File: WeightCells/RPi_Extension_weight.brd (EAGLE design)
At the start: 80 x 50 mm, 32 parts, among them U1 AD7730BRUZ, U2 AD7730BRUZ, U3 AD7730BRUZ, U4 AD7730BRUZ, U5 AD7730BRUZ, U6 AD7730BRUZ, U7 AD7730BRUZ, U8 AD7730BRUZ, U9 STM32F103RCT6

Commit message: updated pcbs
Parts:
- added C10, C9: 0.1uf, rcl:C0603
- renumbered U$1 to Y2, U$2 to Y1
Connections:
- net DVCC: now also C10.1, C9.1
- net GND: now also C10.2, C9.2
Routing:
- net DVCC: track 282.6 -> 286.5 mm
- net U5_AIN1_+: track 24.7 -> 23.6 mm
- net U5_AIN1_-: track 21.9 -> 21.0 mm
- net U6_AIN1_+: track 18.4 -> 17.5 mm
- net +5V: track 151.1 -> 151.8 mm
- net MOSI: track 52.4 -> 51.9 mm

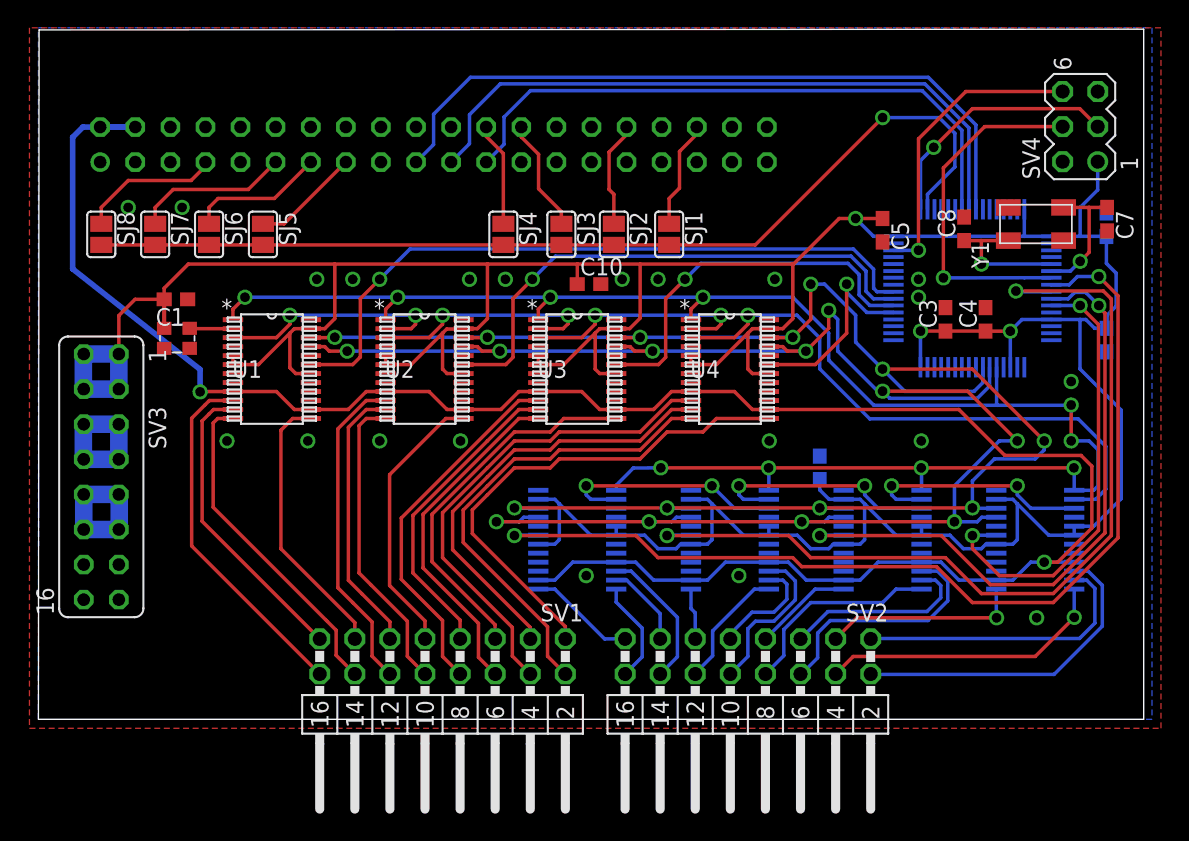
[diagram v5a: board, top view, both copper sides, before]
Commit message: added address lines up to 16 to loadcell board
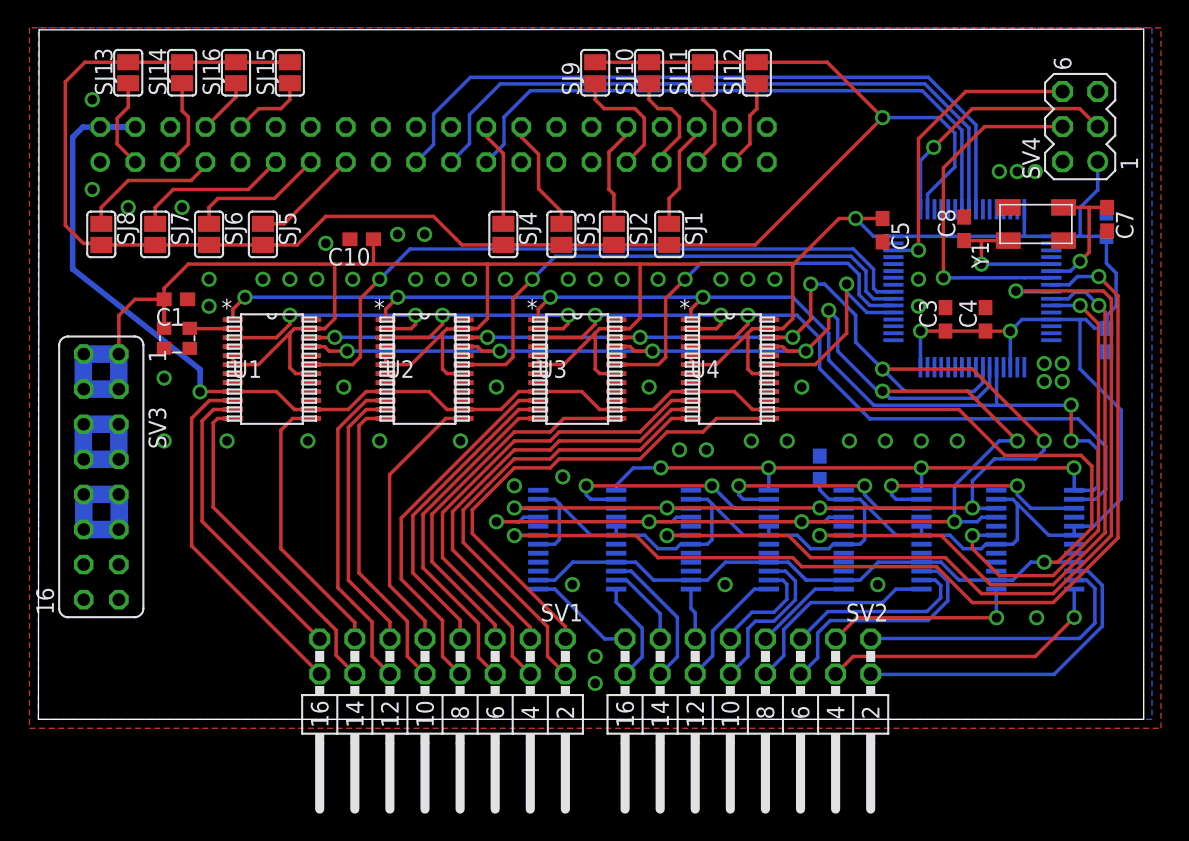
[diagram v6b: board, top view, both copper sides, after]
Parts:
- added SJ10, SJ11, SJ12, SJ13, SJ14, SJ15, SJ16, SJ9: (no value), jumper:SJ
- moved C10 16.8 mm to (23.4, 34.8), turned to 180 degrees
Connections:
- new net N$1: SJ12.1, SV5.37
- new net N$10: SJ14.1, SV5.5
- new net N$4: SJ11.1, SV5.35
- new net N$5: SJ10.1, SV5.33
- new net N$6: SJ9.1, SV5.31
- new net N$7: SJ16.1, SV5.8
- new net N$8: SJ15.1, SV5.10
- new net N$9: SJ13.1, SV5.3
- net SS_STACK: now also SJ10.2, SJ11.2, SJ12.2, SJ13.2, SJ14.2, SJ15.2, SJ16.2, SJ9.2
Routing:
- net SS_STACK: track 72.4 -> 127.0 mm
- net N$6: track 0.00 -> 9.02 mm
- net N$5: track 0.00 -> 7.70 mm
- net N$4: track 0.00 -> 6.60 mm
- net N$9: track 0.00 -> 6.58 mm
- net N$1: track 0.00 -> 6.46 mm
- net N$10: track 0.00 -> 6.43 mm
- net N$8: track 0.00 -> 5.58 mm
- net N$7: track 0.00 -> 4.10 mm

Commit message: created gerber files for adc and load cell board and did some retouch on load cell board
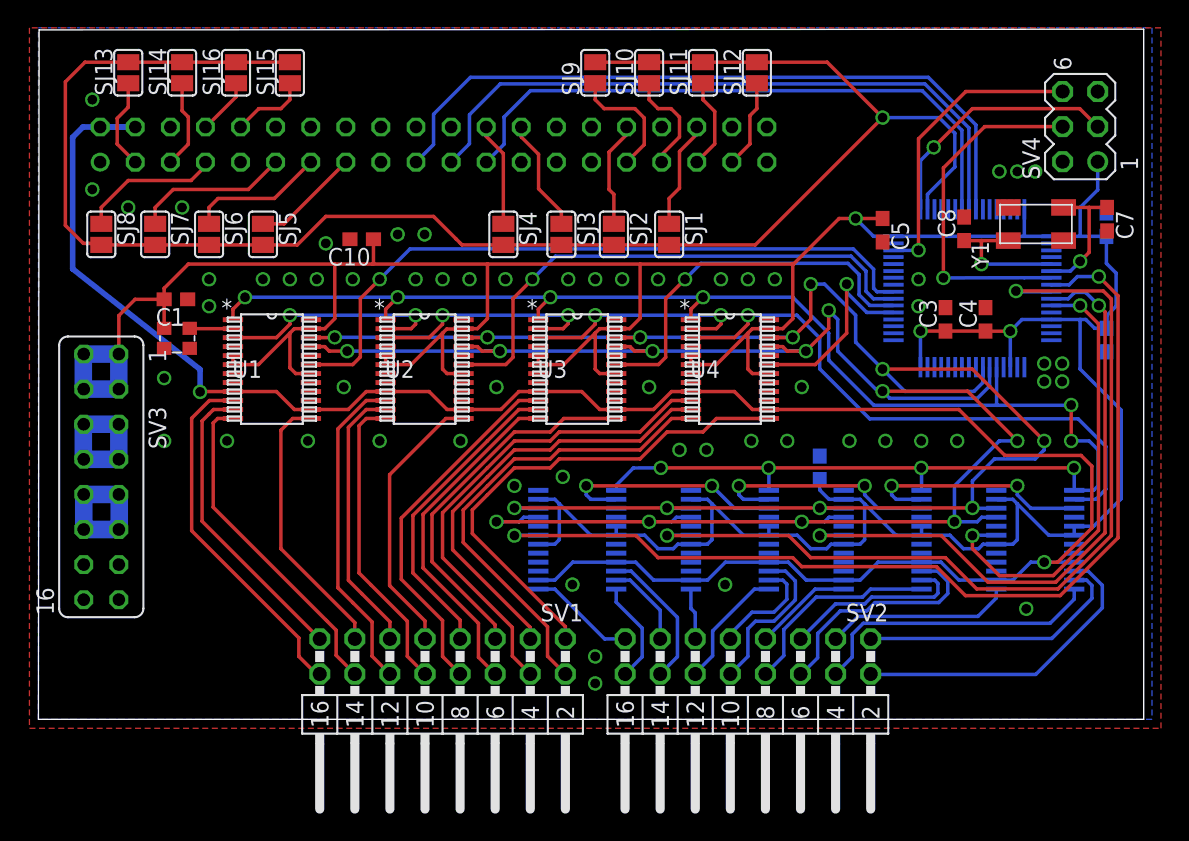
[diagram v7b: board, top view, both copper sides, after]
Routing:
- net U5_AIN1_-: track 21.0 -> 19.6 mm
- net U5_AIN2_-: track 14.4 -> 13.5 mm, vias 1 -> 0
- net U5_AIN1_+: track 23.6 -> 22.9 mm
- net U6_AIN1_-: track 13.8 -> 13.3 mm
- net U5_AIN2_+: track 21.1 -> 21.2 mm, vias 1 -> 0

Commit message: reworked PSU layout
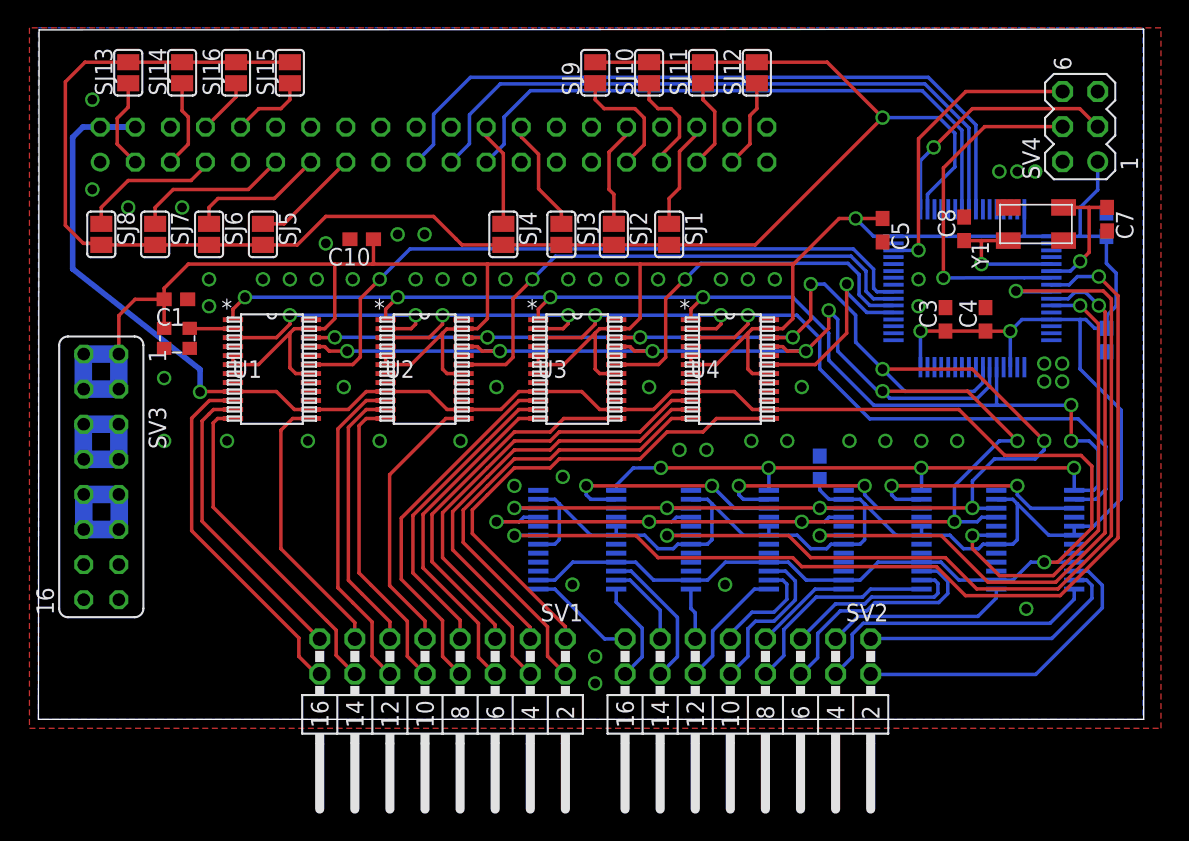
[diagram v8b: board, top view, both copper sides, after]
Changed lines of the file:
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@@
 <vertex x="0" y="0"/>
 <vertex x="0" y="50.05"/>
-<vertex x="80.6" y="50.05"/>
-<vertex x="80.6" y="0"/>
+<vertex x="79.95" y="50.05"/>
+<vertex x="79.95" y="0"/>
 </polygon>
 <contactref element="SV5" pad="25"/>
